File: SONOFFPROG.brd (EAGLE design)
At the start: 15.2 x 29.2 mm, 3 parts, among them SW1 SWITCH-SPDTB

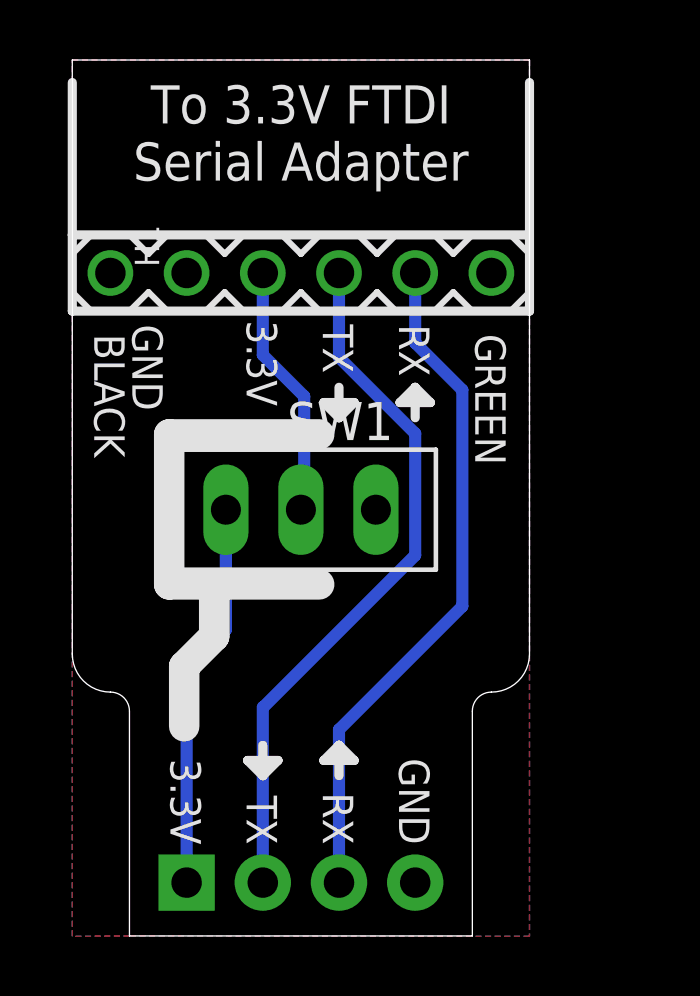
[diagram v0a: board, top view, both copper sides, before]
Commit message: Replaced jumper with NC button, and added GND header for v2.0 release
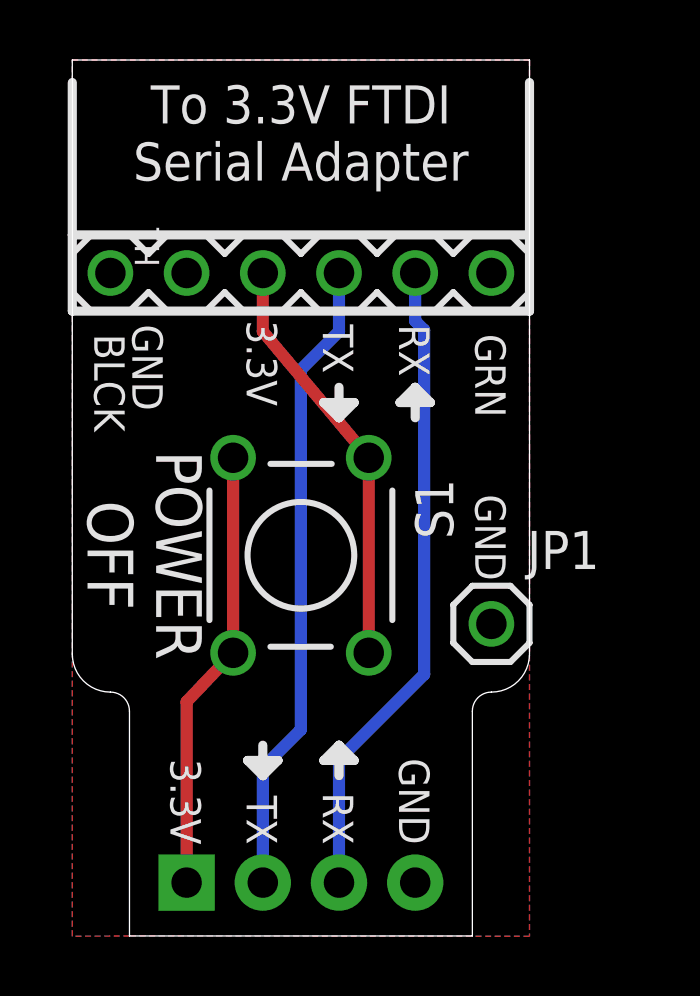
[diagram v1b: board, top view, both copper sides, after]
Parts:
- removed SW1: SWITCH-SPDTB, freetronics-jon:SPDT-2.5MM
- added JP1: M01PTH, freetronics-original:1X01
- added S1: (no value), freetronics-original:TACTILE-PTH
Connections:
- net GND: now also JP1.1
- net N$1: now also S1.3, S1.4; no longer SW1.3
- net N$4: now also S1.1, S1.2; no longer SW1.2
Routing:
- net N$4: track 8.47 -> 13.9 mm
- net TXD: track 23.5 -> 21.4 mm
- net N$1: track 13.0 -> 14.8 mm
- net RXD: track 22.7 -> 21.6 mm
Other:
- board text added: "BLCK"
- board text added: "GRN"
- board text added: "POWER OFF"
- board text added: "v2.0"
- board text removed: "BLACK"
- board text removed: "GREEN"
- board text removed: "v1.0"
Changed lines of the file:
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@@
 <?xml version="1.0" encoding="utf-8"?>
 <!DOCTYPE eagle SYSTEM "eagle.dtd">
-<eagle version="8.6.0">
+<eagle version="9.4.0">
 <drawing>
 <settings>
@@
 <setting verticaltext="up"/>
 </settings>
-<grid distance="1" unitdist="mm" unit="mm" style="lines" multiple="1" display="yes" altdistance="3.125" altunitdist="mil" altunit="mil"/>
+<grid distance="0.05" unitdist="inch" unit="inch" style="lines" multiple="1" display="yes" altdistance="3.125" altunitdist="mil" altunit="mil"/>
 <layers>
 <layer number="1" name="Top" color="4" fill="1" visible="yes" active="yes"/>
@@
 Adapter</text>
 <text x="1.6587" y="10.0962" size="1.016" layer="22" font="vector" ratio="15" rot="SMR90">SKU: SPROG</text>
-<text x="0.73025" y="20.078" size="1.016" layer="21" font="vector" ratio="15" rot="SR270">BLACK</text>
-<text x="13.43025" y="20.078" size="1.016" layer="21" font="vector" ratio="15" rot="SR270">GREEN</text>
+<text x="0.73025" y="20.078" size="1.016" layer="21" font="vector" ratio="15" rot="SR270">BLCK</text>
+<text x="13.43025" y="20.078" size="1.016" layer="21" font="vector" ratio="15" rot="SR270">GRN</text>
 <text x="11.5" y="3.556" size="1.0668" layer="22" font="vector" ratio="15" rot="SMR90">superhouse.tv/sprog</text>
 <text x="5.8103" y="20.53" size="1.016" layer="21" font="vector" ratio="15" rot="SR270">3.3V</text>
@@
 <text x="7.62" y="25.19" size="1.27" layer="21" font="vector" ratio="16" rot="SR0" align="bottom-center">To 3.3V FTDI
 Serial Adapter</text>
-<wire x1="4.73" y1="11.73" x2="4.73" y2="10" width="1.016" layer="21"/>
-<wire x1="4.73" y1="10" x2="3.73" y2="9" width="1.016" layer="21"/>
-<wire x1="3.73" y1="9" x2="3.73" y2="7" width="1.016" layer="21"/>
 <wire x1="8.89" y1="5.354" x2="8.89" y2="6.37" width="0.3048" layer="21"/>
 <wire x1="8.89" y1="6.37" x2="9.398" y2="5.862" width="0.3048" layer="21"/>
@@
 <wire x1="6.858" y1="5.862" x2="5.842" y2="5.862" width="0.3048" layer="21"/>
 <wire x1="5.842" y1="5.862" x2="6.35" y2="5.354" width="0.3048" layer="21"/>
-<wire x1="3.23" y1="11.73" x2="4.73" y2="11.73" width="1.016" layer="21"/>
-<wire x1="4.73" y1="11.73" x2="8.23" y2="11.73" width="1.016" layer="21"/>
-<wire x1="3.23" y1="11.73" x2="3.23" y2="16.73" width="1.016" layer="21"/>
-<wire x1="3.23" y1="16.73" x2="8.23" y2="16.73" width="1.016" layer="21"/>
-<text x="3.7938" y="23.2155" size="1.016" layer="22" font="vector" ratio="15" rot="SMR0">v1.0</text>
+<text x="6.3338" y="19.4055" size="1.016" layer="22" font="vector" ratio="15" rot="SMR0">v2.0</text>
+<text x="0.508" y="12.7" size="1.524" layer="21" font="vector" ratio="18" rot="SR270" align="bottom-center">POWER
+OFF</text>
+<text x="13.4303" y="14.732" size="1.016" layer="21" font="vector" ratio="15" rot="SR270">GND</text>
 </plain>
 <attributes>
@@
 <param name="checkStop" value="0"/>
 <param name="checkValues" value="0"/>
+<param name="checkNames" value="1"/>
+<param name="checkWireStubs" value="1"/>
+<param name="checkPolygonWidth" value="0"/>
 <param name="useDiameter" value="13"/>
 <param name="maxErrors" value="50"/>
@@
 <attribute name="VALUE" x="0" y="18.935" size="1.27" layer="27"/>
 </element>
-<element name="H2" library="freetronics-jon" package="1X04" value="Sonoff" x="3.81" y="1.79" rot="MR180"/>
-<element name="SW1" library="freetronics-jon" package="SPDT-2.5MM" value="SWITCH-SPDTB" x="7.62" y="14.22" rot="R180"/>
+<element name="H2" library="freetronics-jon" package="1X04" value="Sonoff" x="3.81" y="1.79" smashed="yes" rot="MR180">
+<attribute name="NAME" x="2.4638" y="-0.0388" size="1.27" layer="26" ratio="10" rot="MR180"/>
+<attribute name="VALUE" x="2.54" y="4.965" size="1.27" layer="28" rot="MR180"/>
+</element>
+<element name="S1" library="freetronics-original" package="TACTILE-PTH" value="" x="7.62" y="12.7" smashed="yes" rot="R270">
+<attribute name="NAME" x="11.43" y="15.24" size="1.27" layer="25" ratio="10" rot="R270"/>
+</element>
+<element name="JP1" library="freetronics-original" package="1X01" value="M01PTH" x="13.97" y="10.414" smashed="yes">
+<attribute name="NAME" x="15.1638" y="12.2428" size="1.27" layer="25"/>
+<attribute name="VALUE" x="12.7" y="7.239" size="1.27" layer="27"/>
+</element>
 </elements>
 <signals>
@@
 </polygon>
 <contactref element="H2" pad="4"/>
+<contactref element="JP1" pad="1"/>
 </signal>
 <signal name="TXD">
 <contactref element="H1" pad="4"/>
 <contactref element="H2" pad="2"/>
-<wire x1="8.89" y1="22.11" x2="8.89" y2="19.3" width="0.4064" layer="16"/>
-<wire x1="6.35" y1="7.64" x2="6.35" y2="1.79" width="0.4064" layer="16"/>
-<wire x1="11.43" y1="16.76" x2="11.43" y2="12.7" width="0.4064" layer="16"/>
-<wire x1="11.43" y1="12.7" x2="6.37" y2="7.64" width="0.4064" layer="16"/>
-<wire x1="6.37" y1="7.64" x2="6.35" y2="7.64" width="0.3048" layer="16"/>
-<wire x1="8.89" y1="19.3" x2="11.43" y2="16.76" width="0.4064" layer="16"/>
+<wire x1="6.35" y1="5.64" x2="6.35" y2="1.79" width="0.4064" layer="16"/>
+<wire x1="6.35" y1="5.64" x2="6.37" y2="5.64" width="0.3048" layer="16"/>
+<wire x1="8.89" y1="22.11" x2="8.89" y2="20.16" width="0.4064" layer="16"/>
+<wire x1="6.37" y1="5.64" x2="7.62" y2="6.89" width="0.4064" layer="16"/>
+<wire x1="7.62" y1="6.89" x2="7.62" y2="18.89" width="0.4064" layer="16"/>
+<wire x1="7.62" y1="18.89" x2="8.89" y2="20.16" width="0.4064" layer="16"/>
 </signal>
 <signal name="RXD">
 <contactref element="H1" pad="5"/>
 <contactref element="H2" pad="3"/>
-<wire x1="11.43" y1="22.11" x2="11.43" y2="19.78" width="0.4064" layer="16"/>
-<wire x1="11.43" y1="19.78" x2="13" y2="18.21" width="0.4064" layer="16"/>
-<wire x1="13" y1="11" x2="13" y2="18.21" width="0.4064" layer="16"/>
-<wire x1="8.89" y1="6.89" x2="13" y2="11" width="0.4064" layer="16"/>
-<wire x1="8.89" y1="1.79" x2="8.89" y2="6.89" width="0.4064" layer="16"/>
+<wire x1="11.43" y1="22.11" x2="11.43" y2="20.51" width="0.4064" layer="16"/>
+<wire x1="11.43" y1="20.51" x2="11.73" y2="20.21" width="0.4064" layer="16"/>
+<wire x1="11.73" y1="8.73" x2="11.73" y2="20.21" width="0.4064" layer="16"/>
+<wire x1="8.89" y1="5.89" x2="11.73" y2="8.73" width="0.4064" layer="16"/>
+<wire x1="8.89" y1="1.79" x2="8.89" y2="5.89" width="0.4064" layer="16"/>
 </signal>
 <signal name="N$1">
 <contactref element="H2" pad="1"/>
-<contactref element="SW1" pad="3"/>
-<wire x1="3.81" y1="1.79" x2="3.81" y2="8.91" width="0.4064" layer="16"/>
-<wire x1="3.81" y1="8.91" x2="5.12" y2="10.22" width="0.4064" layer="16"/>
-<wire x1="5.12" y1="10.22" x2="5.12" y2="14.22" width="0.4064" layer="16"/>
+<contactref element="S1" pad="4"/>
+<contactref element="S1" pad="3"/>
+<wire x1="5.3594" y1="15.9512" x2="5.3594" y2="9.4488" width="0.4064" layer="1"/>
+<wire x1="5.3594" y1="9.4488" x2="3.81" y2="7.8194" width="0.4064" layer="1"/>
+<wire x1="3.81" y1="7.8194" x2="3.81" y2="1.79" width="0.4064" layer="1"/>
 </signal>
 <signal name="N$4">
 <contactref element="H1" pad="3"/>
-<contactref element="SW1" pad="2"/>
-<wire x1="6.35" y1="22.11" x2="6.35" y2="19.38" width="0.4064" layer="16"/>
-<wire x1="6.35" y1="19.38" x2="7.73" y2="18" width="0.4064" layer="16"/>
-<wire x1="7.73" y1="18" x2="7.73" y2="15.6" width="0.4064" layer="16"/>
-<wire x1="7.73" y1="15.6" x2="7.62" y2="14.22" width="0.3048" layer="16"/>
+<contactref element="S1" pad="2"/>
+<contactref element="S1" pad="1"/>
+<wire x1="6.35" y1="22.11" x2="6.35" y2="20.1618" width="0.4064" layer="1"/>
+<wire x1="6.35" y1="20.1618" x2="9.8806" y2="15.9512" width="0.4064" layer="1"/>
+<wire x1="9.8806" y1="15.9512" x2="9.8806" y2="9.4488" width="0.4064" layer="1"/>
 </signal>
 </signals>
+<mfgpreviewcolors>
+<mfgpreviewcolor name="soldermaskcolor" color="0xC8008000"/>
+<mfgpreviewcolor name="silkscreencolor" color="0xFFFEFEFE"/>
+<mfgpreviewcolor name="backgroundcolor" color="0xFF282828"/>
+<mfgpreviewcolor name="coppercolor" color="0xFFFFBF00"/>
+<mfgpreviewcolor name="substratecolor" color="0xFF786E46"/>
+</mfgpreviewcolors>
 </board>
 </drawing>
